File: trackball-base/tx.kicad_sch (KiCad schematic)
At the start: 29 parts, among them U501 LTC4125EUFD

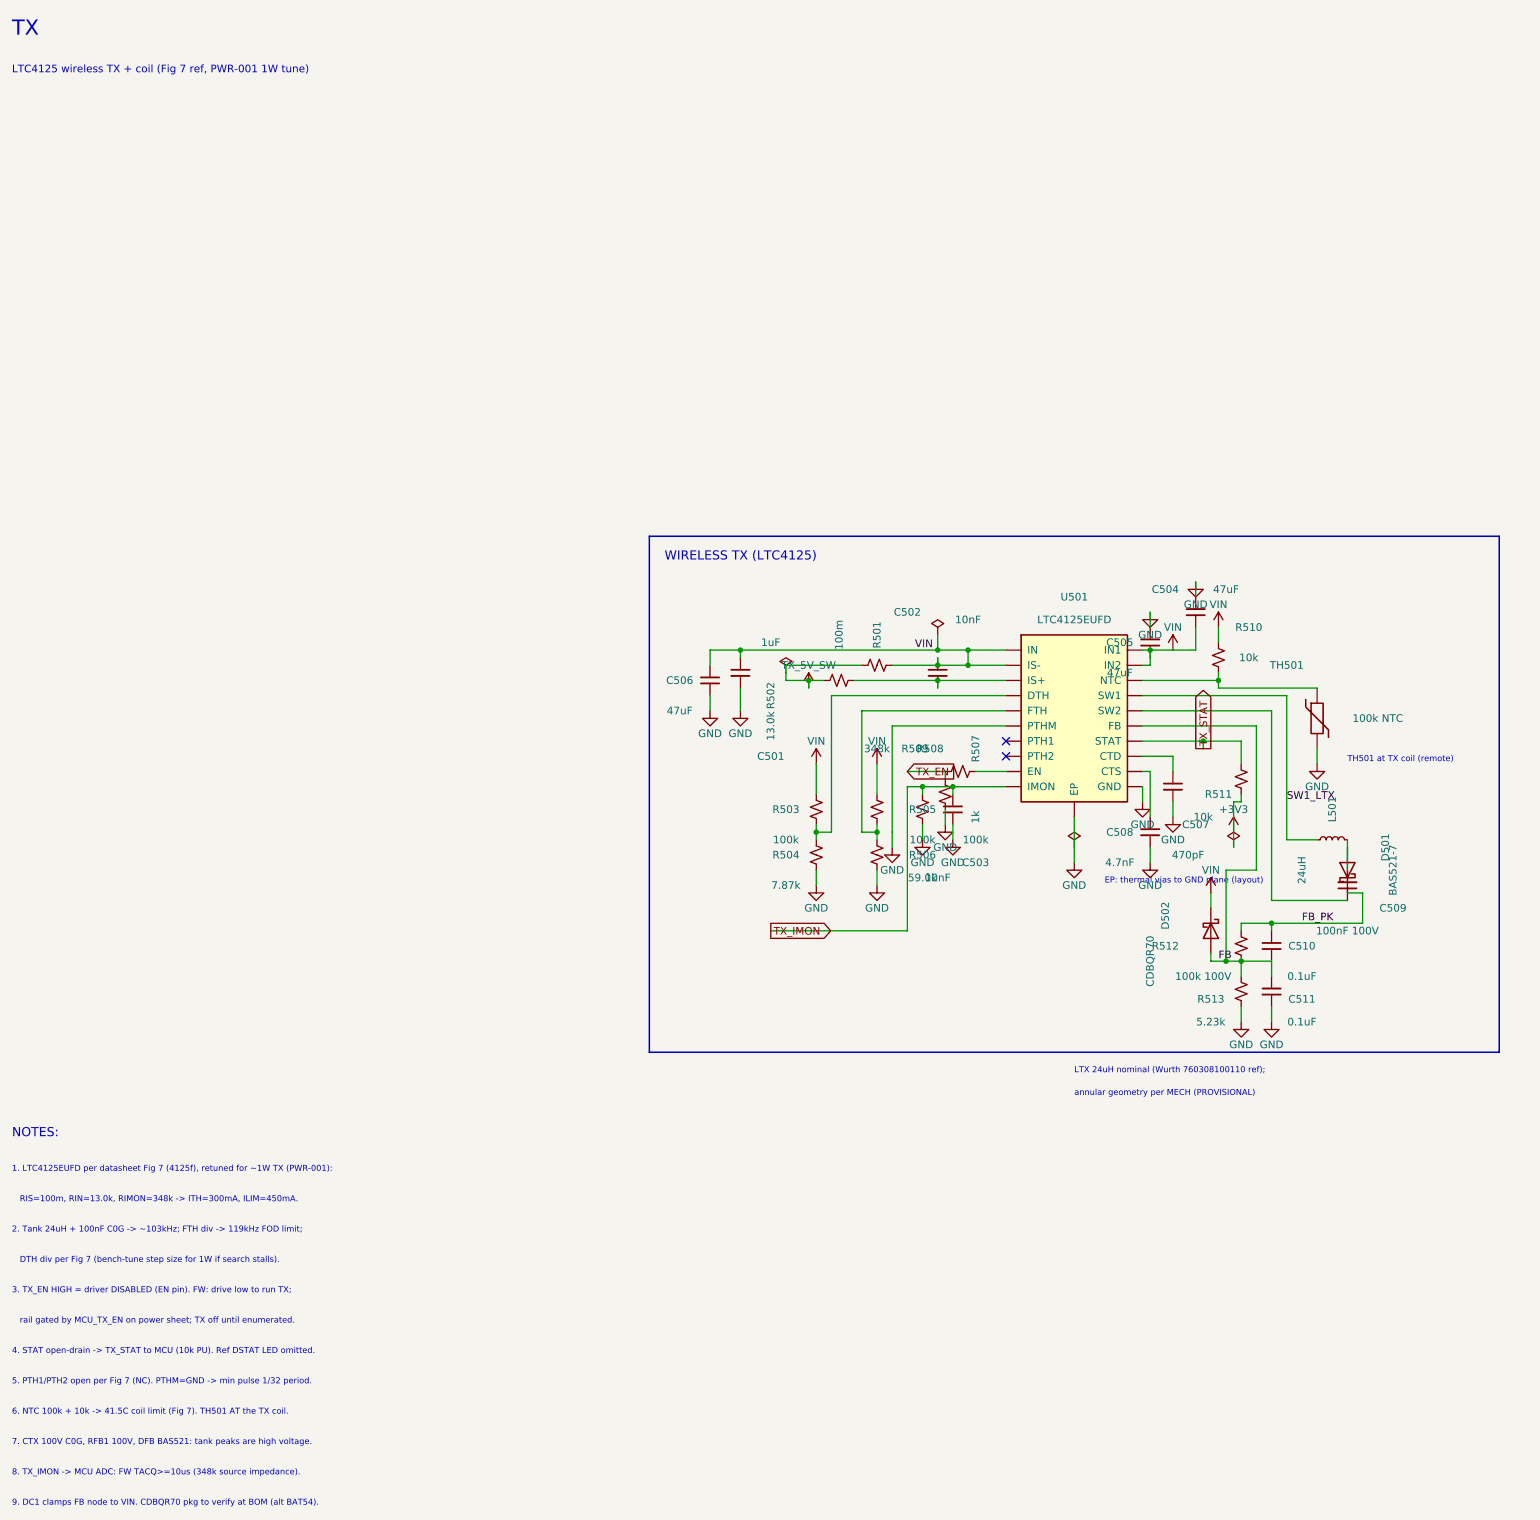
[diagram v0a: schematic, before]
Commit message: base schematic complete: root + 5 sheets ERC-clean, review notes + BOM draft
Full hierarchical project (root + power/mcu/sensors/buttons/tx):
0 ERC errors, 1 benign pin_to_pin warning (ADC rail-sense, documented).
Netlist-verified: 145 comps, VSEN_1V9/MCU_RST/USB/SPI/TX nets.
Adds notes/SCHEMATIC_REVIEW.md (decisions, rail design, TX tree,
antenna, GPIO map, provisionals, ERC log) + notes/BOM_DRAFT.md.
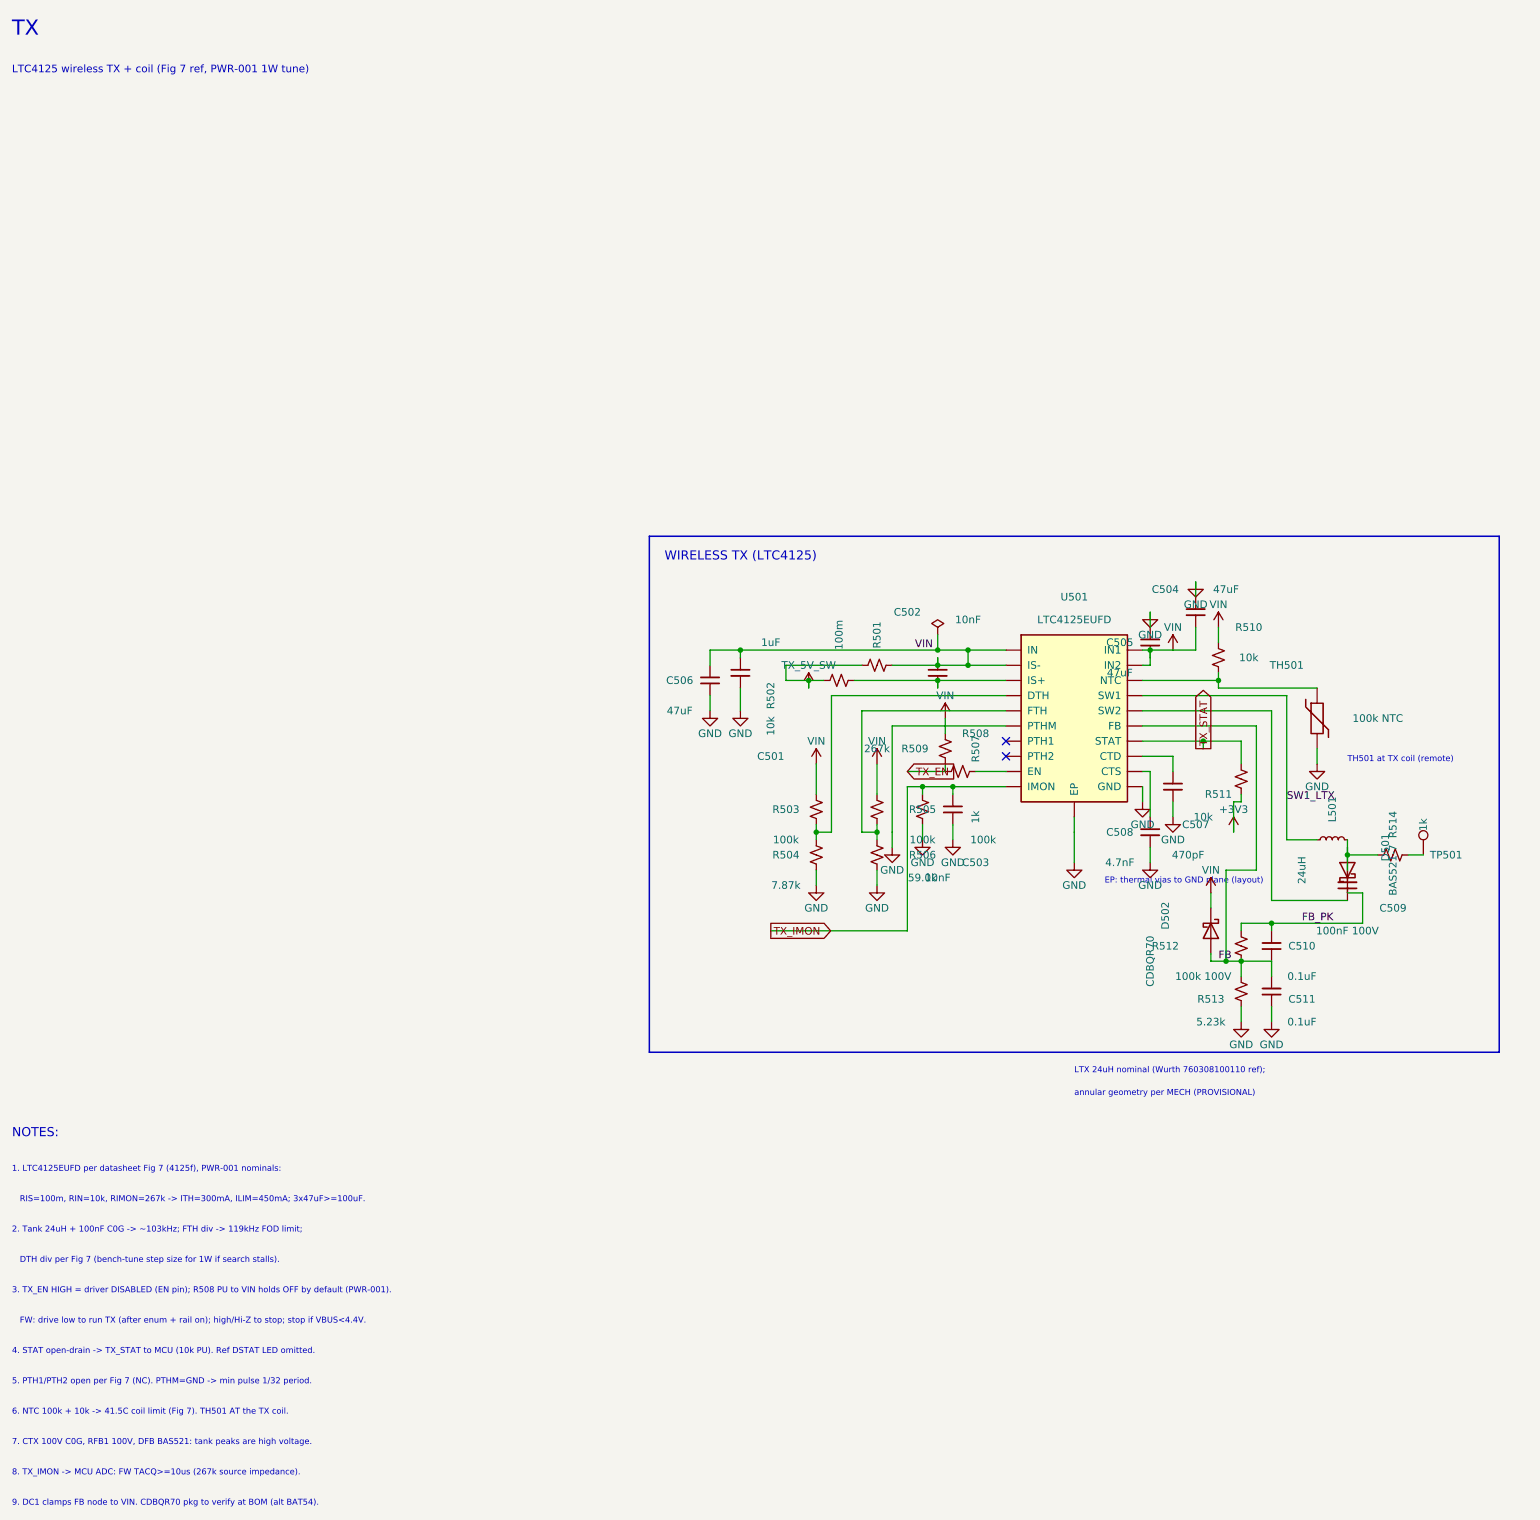
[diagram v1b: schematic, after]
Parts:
- added R514: 1k, Resistor_SMD:R_0402_1005Metric, symbol Device:R_Small_US
- added TP501: TP501, TestPoint:TestPoint_Pad_D1.5mm, symbol Connector:TestPoint
- D502: footprint Diode_SMD:D_SOD-123 -> Diode_SMD:D_0402_1005Metric
- R502: value 13.0k -> 10k
- R509: value 348k -> 267k
- U501: footprint (none) -> Package_DFN_QFN:QFN-20-1EP_4x4mm_P0.5mm_EP2.5x2.5mm_ThermalVias
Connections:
- net GND: no longer R508.2
- net TX_EN: now also R508.2; no longer R508.1
- net VIN: now also R508.1
- net at C509.1, D501.2 (A), L501.2: now also R514.1
- new net: R514.2, TP501.1
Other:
- note added: "1. LTC4125EUFD per datasheet Fig 7 (4125f), PWR-001 nominals:"
- note added: "3. TX_EN HIGH = driver DISABLED (EN pin); R508 PU to VIN holds OFF by default (PWR-001)."
- note added: "8. TX_IMON -> MCU ADC: FW TACQ>=10us (267k source impedance)."
- note added: "FW: drive low to run TX (after enum + rail on); high/Hi-Z to stop; stop if VBUS<4.4V."
- note added: "RIS=100m, RIN=10k, RIMON=267k -> ITH=300mA, ILIM=450mA; 3x47uF>=100uF."
- note removed: "1. LTC4125EUFD per datasheet Fig 7 (4125f), retuned for ~1W TX (PWR-001):"
- note removed: "3. TX_EN HIGH = driver DISABLED (EN pin). FW: drive low to run TX;"
- note removed: "8. TX_IMON -> MCU ADC: FW TACQ>=10us (348k source impedance)."
- note removed: "RIS=100m, RIN=13.0k, RIMON=348k -> ITH=300mA, ILIM=450mA."
- note removed: "rail gated by MCU_TX_EN on power sheet; TX off until enumerated."

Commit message: layout: placed+silk+parity-0 (drc10: 0 errors/0 parity, 125 warnings)
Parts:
- L501: footprint (none) -> trackball:TX_COIL_IF_2P508
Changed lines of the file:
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@@
         ))
     )
-    (property "Footprint" ""
+    (property "Footprint" "trackball:TX_COIL_IF_2P508"
       (at 233.68 147.32 0)
       (effects (font (size 1.27 1.27)) hide)
@@
       (at 233.68 147.32 0)
       (effects (font (size 1.27 1.27)) hide)
+    )
+    (property "Description" "TX coil 2-pin interface"
+      (at 233.68 147.32 0)
+      (effects (font (size 1.27 1.27)) hide)

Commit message: WIP routing drc143: unc 57, 0 viol, VBUS12/GND11
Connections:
- net Net-(U501-IS+): now reaches C502.2, R502.2, U501.4 (IS+)
- net Net-(U501-CTD): now reaches C507.1, U501.14 (CTD)
- net Net-(U501-EN): now reaches R507.2, U501.15 (EN)
- net Net-(U501-SW2): now reaches C509.2, U501.18 (SW2)
- net Net-(U501-CTS): now reaches C508.1, U501.2 (CTS)
- net Net-(U501-NTC): now reaches R510.2, TH501.1, U501.6 (NTC)
- net Net-(U501-DTH): now reaches R503.2, R504.1, U501.7 (DTH)
- net Net-(U501-FTH): now reaches R505.2, R506.1, U501.9 (FTH)
- net Net-(D501-A): now reaches C509.1, D501.2 (A), L501.2, R514.1
- net Net-(R514-Pad2): now reaches R514.2, TP501.1
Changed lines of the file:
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@@
     (color 0 0 0 0)
   )
+  (label "Net-(D501-A)"
+    (at 236.22 152.40 90)
+    (effects
+        (font
+          (size 1.27 1.27)
+        )
+        (justify left bottom))
+  )
+  (label "Net-(R514-Pad2)"
+    (at 246.38 149.86 0)
+    (effects
+        (font
+          (size 1.27 1.27)
+        )
+        (justify left bottom))
+  )
+  (label "Net-(U501-CTD)"
+    (at 207.01 135.89 90)
+    (effects
+        (font
+          (size 1.27 1.27)
+        )
+        (justify left bottom))
+  )
+  (label "Net-(U501-CTS)"
+    (at 203.20 143.51 90)
+    (effects
+        (font
+          (size 1.27 1.27)
+        )
+        (justify left bottom))
+  )
+  (label "Net-(U501-DTH)"
+    (at 147.32 144.78 90)
+    (effects
+        (font
+          (size 1.27 1.27)
+        )
+        (justify left bottom))
+  )
+  (label "Net-(U501-EN)"
+    (at 173.99 135.89 0)
+    (effects
+        (font
+          (size 1.27 1.27)
+        )
+        (justify left bottom))
+  )
+  (label "Net-(U501-FTH)"
+    (at 157.48 144.78 90)
+    (effects
+        (font
+          (size 1.27 1.27)
+        )
+        (justify left bottom))
+  )
+  (label "Net-(U501-IS+)"
+    (at 167.64 121.92 90)
+    (effects
+        (font
+          (size 1.27 1.27)
+        )
+        (justify left bottom))
+  )
+  (label "Net-(U501-NTC)"
+    (at 214.63 119.38 90)
+    (effects
+        (font
+          (size 1.27 1.27)
+        )
+        (justify left bottom))
+  )
+  (label "Net-(U501-SW2)"
+    (at 236.22 157.48 0)
+    (effects
+        (font
+          (size 1.27 1.27)
+        )
+        (justify left bottom))
+  )
 )

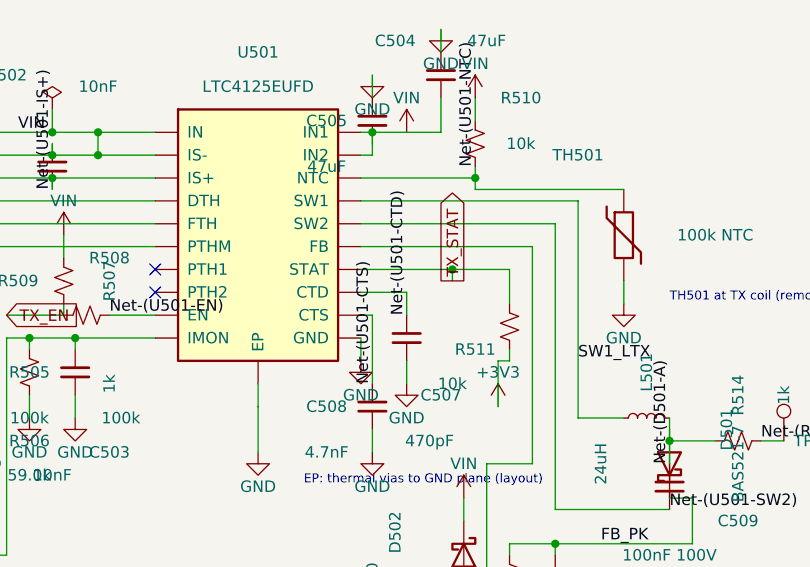
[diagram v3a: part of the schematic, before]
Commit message: Q5 ECO + pre-ripup checkpoint: R113/114/115/515 jumpers, drc129 33unc/0err/0parity
Schematic (owner-approved 2026-10-04): 3x 0R branch jumpers on power
sheet (R113 VBUS_SENSE, R114 SENSOR_EN, R115 MCU_TX_EN) + R515 CTD
in-line on tx (net split /tx/CTD_U501 + /tx/Net-(U501-CTD)). ERC 0
errors + 1 known benign warning; netlist diff minimal (4 nets only).
PCB: 4x 0603 staged, nets assigned, U501.14 on CTD_U501; 0 parity.
Docs: SCHEMATIC_REVIEW §11, BOM row, LAYOUT_REVIEW E53, QUESTIONS.
Reversible checkpoint before Q6 ripup.
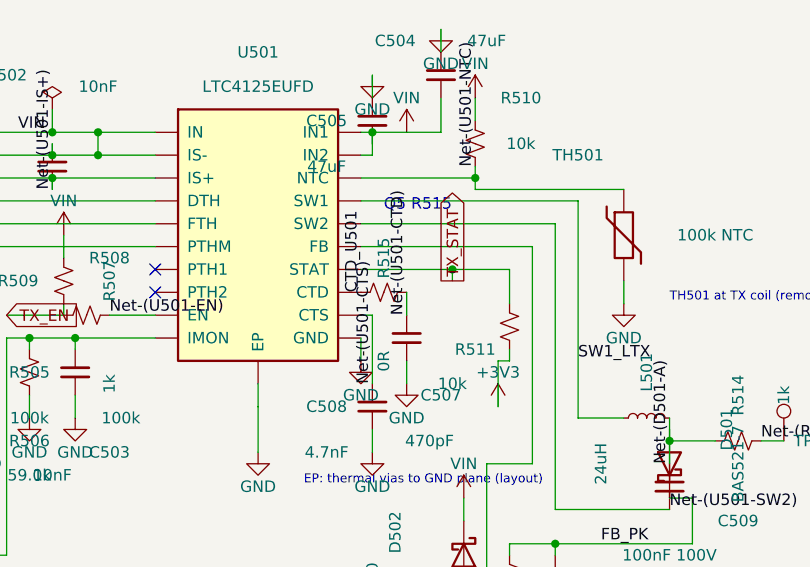
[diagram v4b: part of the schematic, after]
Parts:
- added R515: 0R, Resistor_SMD:R_0603_1608Metric, symbol Device:R_Small_US
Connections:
- net Net-(U501-CTD): now also R515.2; no longer U501.14 (CTD)
- new net CTD_U501: R515.1, U501.14 (CTD)
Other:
- note added: "Q5 R515"
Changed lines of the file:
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@@
-  )
-  (wire
-    (pts (xy 201.93 133.35) (xy 207.01 133.35))
-    (stroke (width 0) (type default))
   )
   (wire
@@
     (effects
         (font
+          (size 1.27 1.27)
+        )
+        (justify left bottom))
+  )
+  (symbol
+    (lib_id "Device:R_Small_US")
+    (at 204.47 133.35 90)
+    (unit 1)
+    (exclude_from_sim no)
+    (in_bom yes)
+    (on_board yes)
+    (fields_autoplaced yes)
+    (property "Reference" "R515"
+      (at 204.47 129.54 0)
+      (effects
+        (font
+          (size 1.27 1.27)
+        ))
+    )
+    (property "Value" "0R"
+      (at 204.47 141.00 0)
+      (effects
+        (font
+          (size 1.27 1.27)
+        ))
+    )
+    (property "Footprint" "Resistor_SMD:R_0603_1608Metric"
+      (at 204.47 133.35 0)
+      (effects (font (size 1.27 1.27)) hide)
+    )
+    (property "Datasheet" ""
+      (at 204.47 133.35 0)
+      (effects (font (size 1.27 1.27)) hide)
+    )
+    (pin "1")
+    (pin "2")
+  )
+  (text "Q5 R515"
+    (at 204.47 124.46 0)
+    (effects
+        (font
+          (size 1.27 1.27)
+        )
+        (justify left bottom))
+  )
+  (label "CTD_U501"
+    (at 201.93 133.35 90)
+    (effects
+        (font
